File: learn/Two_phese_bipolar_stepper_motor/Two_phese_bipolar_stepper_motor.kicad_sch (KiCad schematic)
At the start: 15 parts

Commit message: 21/02/23 inserito tutti i componenti necessari per il nuovo progetto.
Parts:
- added U?: L297, symbol Driver_Motor:L297
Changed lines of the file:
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@@
     (pin "2")
+  )
+  (symbol (lib_id "Driver_Motor:L297") (at 119.38 99.06 0) (unit 1)
+    (in_bom yes) (on_board yes) (fields_autoplaced)
+    (property "Reference" "U?" (id 0) (at 121.3994 116.84 0)
+      (effects (font (size 1.27 1.27)) (justify left))
+    )
+    (property "Value" "L297" (id 1) (at 121.3994 119.38 0)
+      (effects (font (size 1.27 1.27)) (justify left))
+    )
+    (property "Footprint" "" (id 2) (at 113.03 82.55 0)
+      (effects (font (size 1.27 1.27)) hide)
+    )
+    (property "Datasheet" "www.st.com/resource/en/datasheet/cd00000063.pdf" (id 3) (at 113.03 82.55 0)
+      (effects (font (size 1.27 1.27)) hide)
+    )
+    (pin "11")
+    (pin "12")
+    (pin "13")
+    (pin "14")
+    (pin "15")
+    (pin "16")
+    (pin "17")
+    (pin "18")
+    (pin "19")
+    (pin "20")
+    (pin "1")
+    (pin "10")
+    (pin "2")
+    (pin "3")
+    (pin "4")
+    (pin "5")
+    (pin "6")
+    (pin "7")
+    (pin "8")
+    (pin "9")
   )
   (symbol (lib_id "Device:C") (at 212.09 53.34 0) (unit 1)
@@
       (reference "R?") (unit 1) (value "R") (footprint "")
     )
+    (path "/b420444f-520c-4962-ac46-908b94e46b38"
+      (reference "U?") (unit 1) (value "L297") (footprint "")
+    )
   )

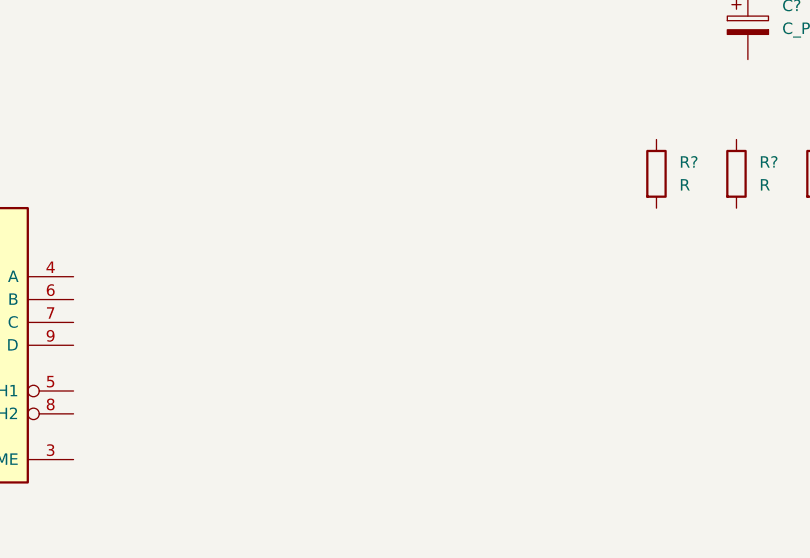
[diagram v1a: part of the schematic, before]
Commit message: 22/02/23 L298N
Ora sono presenti tutti i componenti per creare il progetto.
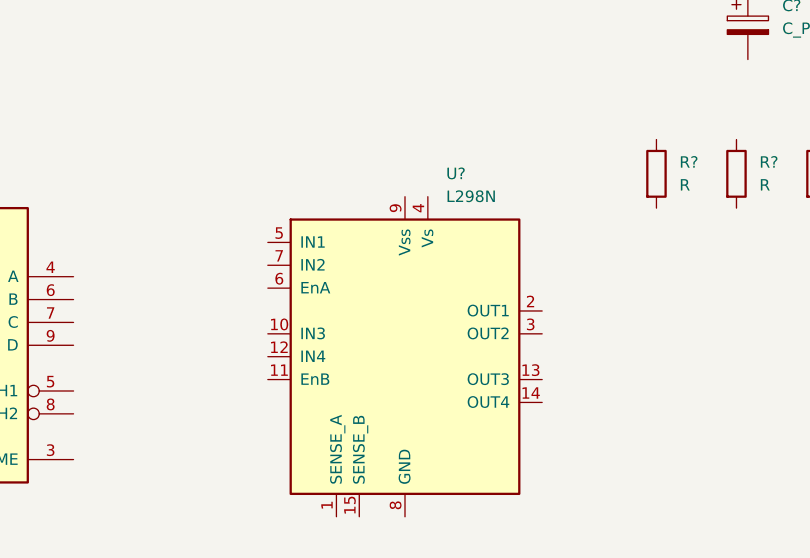
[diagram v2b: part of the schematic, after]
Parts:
- added U?: L298N, Package_TO_SOT_THT:TO-220-15_P2.54x2.54mm_StaggerOdd_Lead4.58mm_Vertical, symbol Driver_Motor:L298N
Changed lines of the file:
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@@
     (pin "2")
+  )
+  (symbol (lib_id "Driver_Motor:L298N") (at 173.99 100.33 0) (unit 1)
+    (in_bom yes) (on_board yes) (fields_autoplaced)
+    (property "Reference" "U?" (id 0) (at 178.5494 80.01 0)
+      (effects (font (size 1.27 1.27)) (justify left))
+    )
+    (property "Value" "L298N" (id 1) (at 178.5494 82.55 0)
+      (effects (font (size 1.27 1.27)) (justify left))
+    )
+    (property "Footprint" "Package_TO_SOT_THT:TO-220-15_P2.54x2.54mm_StaggerOdd_Lead4.58mm_Vertical" (id 2) (at 175.26 116.84 0)
+      (effects (font (size 1.27 1.27)) (justify left) hide)
+    )
+    (property "Datasheet" "http://www.st.com/st-web-ui/static/active/en/resource/technical/document/datasheet/CD00000240.pdf" (id 3) (at 177.8 93.98 0)
+      (effects (font (size 1.27 1.27)) hide)
+    )
+    (pin "1")
+    (pin "10")
+    (pin "11")
+    (pin "12")
+    (pin "13")
+    (pin "14")
+    (pin "15")
+    (pin "2")
+    (pin "3")
+    (pin "4")
+    (pin "5")
+    (pin "6")
+    (pin "7")
+    (pin "8")
+    (pin "9")
   )
   (symbol (lib_id "Device:D_Schottky") (at 137.16 46.99 0) (unit 1)
@@
       (reference "U?") (unit 1) (value "L297") (footprint "")
     )
+    (path "/e37ffe64-a844-4622-840a-a53a0744ab08"
+      (reference "U?") (unit 1) (value "L298N") (footprint "Package_TO_SOT_THT:TO-220-15_P2.54x2.54mm_StaggerOdd_Lead4.58mm_Vertical")
+    )
   )

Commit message: 25/02/23 Inizio collegamento (shc)
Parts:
- C1: renamed from C?; value C -> 3.3nF
- C2, C3: renamed from C?; value C -> 100nF
- C4: renamed from C?; value C_Polarized -> 470uF
- R1: renamed from R?; value R -> 22k
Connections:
- net OSC: now reaches R1.1
- net OSC: now also C1.1
- net VSS: now reaches R1.2
- net VSS: now also C2.1
- net VS: now reaches C4.1
- net VS: now also C3.1
- net GND: now reaches C4.2
- net GND: now also C1.2, C2.2, C3.2
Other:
- moved on the sheet: C1, C2, C3, C4, R1, R?

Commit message: 01/03/23 aggiunto PWR_FLAG
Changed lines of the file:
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@@
   (junction (at 251.46 78.74) (diameter 0) (color 0 0 0 0)
   )
+  (junction (at 214.63 93.98) (diameter 0) (color 0 0 0 0)
+  )
   (junction (at 203.2 81.28) (diameter 0) (color 0 0 0 0)
   )
@@
   (junction (at 218.44 81.28) (diameter 0) (color 0 0 0 0)
   )
+  (junction (at 251.46 76.2) (diameter 0) (color 0 0 0 0)
+  )
+  (junction (at 218.44 80.01) (diameter 0) (color 0 0 0 0)
+  )
   (junction (at 214.63 91.44) (diameter 0) (color 0 0 0 0)
   )
@@
     (stroke (width 0) (type default) (color 0 0 0 0))
   )
+  (wire (pts (xy 245.11 76.2) (xy 251.46 76.2))
+    (stroke (width 0) (type default) (color 0 0 0 0))
+  )
   (wire (pts (xy 242.57 78.74) (xy 251.46 78.74))
     (stroke (width 0) (type default) (color 0 0 0 0))
@@
     (stroke (width 0) (type default) (color 0 0 0 0))
   )
+  (wire (pts (xy 209.55 93.98) (xy 214.63 93.98))
+    (stroke (width 0) (type default) (color 0 0 0 0))
+  )
   (wire (pts (xy 214.63 91.44) (xy 214.63 93.98))
+    (stroke (width 0) (type default) (color 0 0 0 0))
+  )
+  (wire (pts (xy 218.44 80.01) (xy 224.79 80.01))
     (stroke (width 0) (type default) (color 0 0 0 0))
   )
@@
     (pin "2")
   )
+  (symbol (lib_id "power:PWR_FLAG") (at 224.79 80.01 0) (unit 1)
+    (in_bom yes) (on_board yes)
+    (property "Reference" "#FLG?" (id 0) (at 224.79 78.105 0)
+      (effects (font (size 1.27 1.27)) hide)
+    )
+    (property "Value" "PWR_FLAG" (id 1) (at 222.25 76.2 0)
+      (effects (font (size 0.8 0.8)) (justify left))
+    )
+    (property "Footprint" "" (id 2) (at 224.79 80.01 0)
+      (effects (font (size 1.27 1.27)) hide)
+    )
+    (property "Datasheet" "~" (id 3) (at 224.79 80.01 0)
+      (effects (font (size 1.27 1.27)) hide)
+    )
+    (pin "1")
+  )
   (symbol (lib_id "Device:R") (at 209.55 81.28 90) (unit 1)
     (in_bom yes) (on_board yes) (fields_autoplaced)
@@
     (pin "1")
     (pin "2")
+  )
+  (symbol (lib_id "power:PWR_FLAG") (at 245.11 76.2 0) (unit 1)
+    (in_bom yes) (on_board yes) (fields_autoplaced)
+    (property "Reference" "#FLG?" (id 0) (at 245.11 74.295 0)
+      (effects (font (size 1.27 1.27)) hide)
+    )
+    (property "Value" "PWR_FLAG" (id 1) (at 245.11 71.12 0))
+    (property "Footprint" "" (id 2) (at 245.11 76.2 0)
+      (effects (font (size 1.27 1.27)) hide)
+    )
+    (property "Datasheet" "~" (id 3) (at 245.11 76.2 0)
+      (effects (font (size 1.27 1.27)) hide)
+    )
+    (pin "1")
   )
   (symbol (lib_id "power:VSS") (at 218.44 80.01 0) (unit 1)
@@
     (pin "2")
   )
+  (symbol (lib_id "power:PWR_FLAG") (at 209.55 93.98 180) (unit 1)
+    (in_bom yes) (on_board yes)
+    (property "Reference" "#FLG?" (id 0) (at 209.55 95.885 0)
+      (effects (font (size 1.27 1.27)) hide)
+    )
+    (property "Value" "PWR_FLAG" (id 1) (at 212.09 97.79 0)
+      (effects (font (size 0.8 0.8)) (justify left))
+    )
+    (property "Footprint" "" (id 2) (at 209.55 93.98 0)
+      (effects (font (size 1.27 1.27)) hide)
+    )
+    (property "Datasheet" "~" (id 3) (at 209.55 93.98 0)
+      (effects (font (size 1.27 1.27)) hide)
+    )
+    (pin "1")
+  )
   (sheet_instances
     (path "/" (page "1"))
   )
   (symbol_instances
+    (path "/3e6463cb-88fe-4589-b0c8-c0269a2931ca"
+      (reference "#FLG?") (unit 1) (value "PWR_FLAG") (footprint "")
+    )
+    (path "/6791b6c4-8825-4d77-97a1-1f490967f6cd"
+      (reference "#FLG?") (unit 1) (value "PWR_FLAG") (footprint "")
+    )
+    (path "/fbbf62bf-eae9-4a55-9a35-5a034367347f"
+      (reference "#FLG?") (unit 1) (value "PWR_FLAG") (footprint "")
+    )
     (path "/2c34f367-ff20-455d-af43-7cdb3c218d3c"
       (reference "#PWR?") (unit 1) (value "GND") (footprint "")

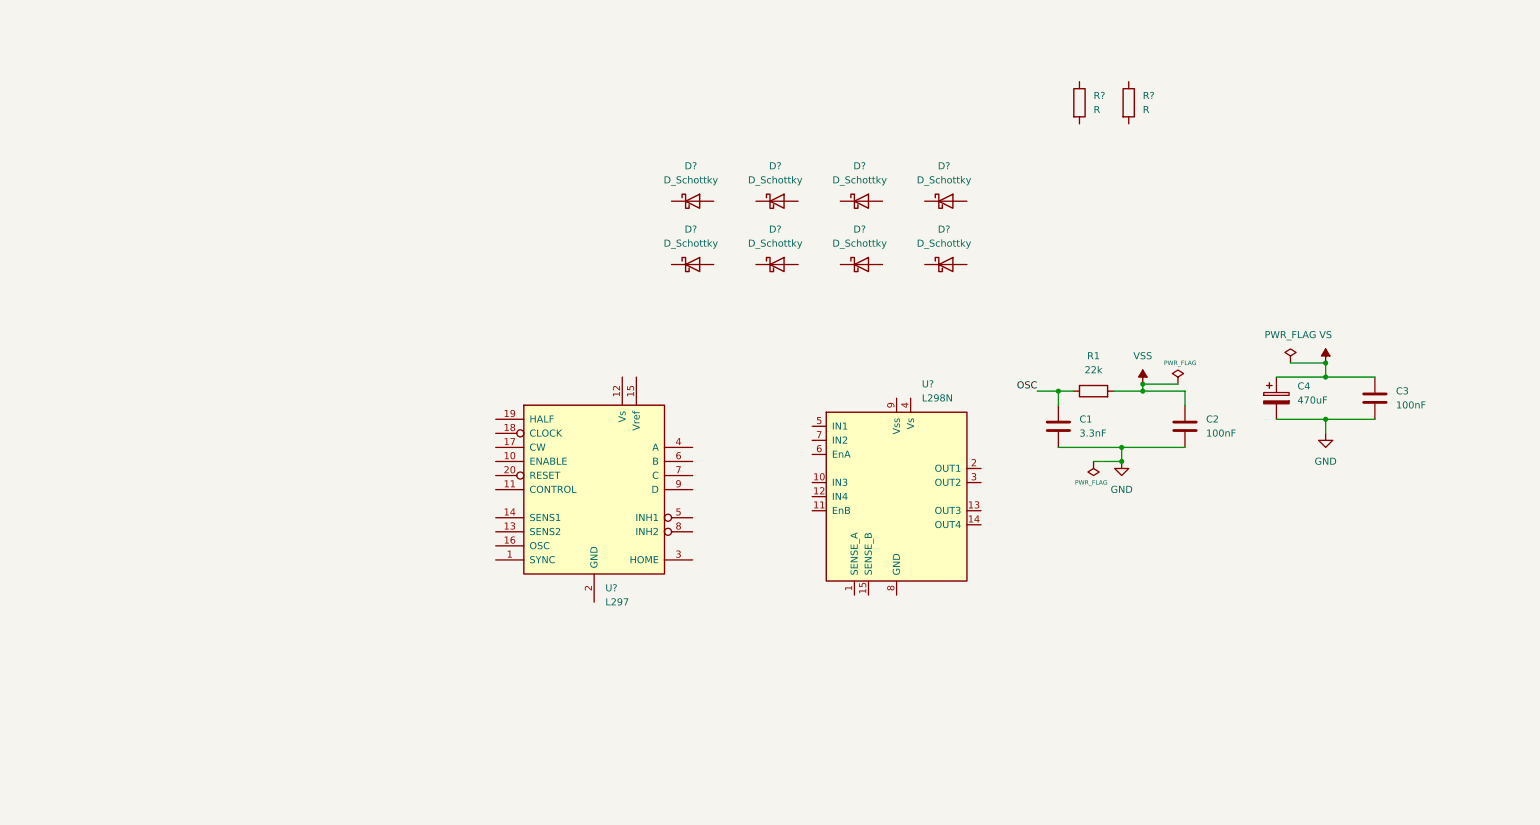
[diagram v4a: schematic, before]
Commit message: 02/03/23 aggiunti diodi Zener
Inizio collegamento del L298N
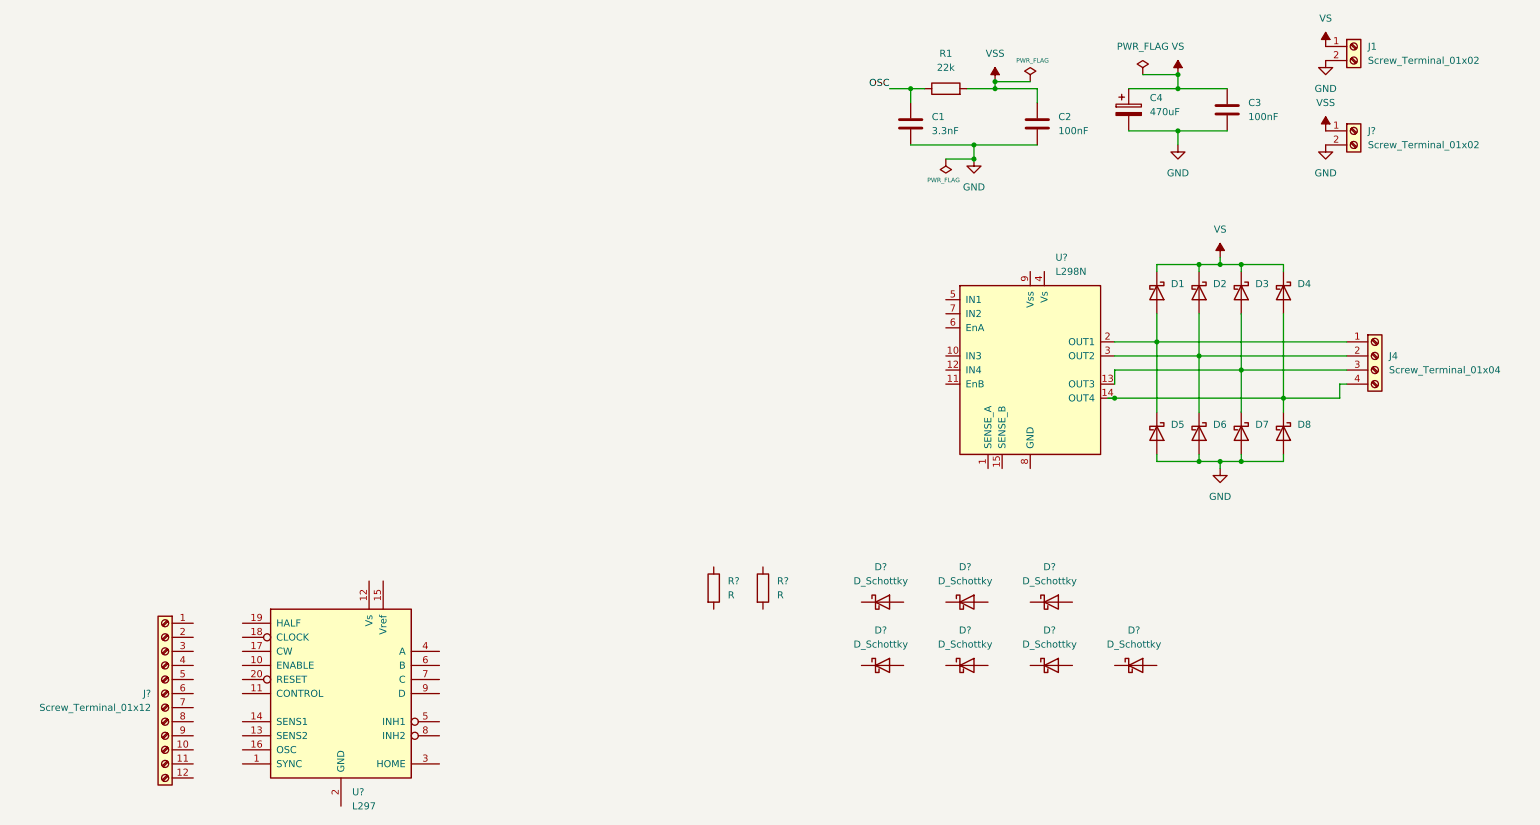
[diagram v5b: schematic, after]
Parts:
- added D2, D3, D4, D5, D6, D7, D8: (no value), symbol Device:D_Schottky
- added J1, J?: Screw_Terminal_01x02, symbol Connector:Screw_Terminal_01x02
- added J4: Screw_Terminal_01x04, symbol Connector:Screw_Terminal_01x04
- added J?: Screw_Terminal_01x12, symbol Connector:Screw_Terminal_01x12
- D1: renamed from D?; value D_Schottky -> (none)
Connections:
- net GND: now also D5.2 (A), D6.2 (A), D7.2 (A), D8.2 (A), J1.2 (Pin_2), J?.2 (Pin_2)
- net VS: now also D1.1 (K), D2.1 (K), D3.1 (K), D4.1 (K), J1.1 (Pin_1)
- net VSS: now also J?.1 (Pin_1)
- net at D1.2 (A): now also U?.2 (OUT1), D5.1 (K), J4.1 (Pin_1)
- net at U?.13 (OUT3): now also D3.2 (A), D7.1 (K), J4.3 (Pin_3)
- net at U?.14 (OUT4): now also D4.2 (A), D8.1 (K), J4.4 (Pin_4)
- net at U?.3 (OUT2): now also D2.2 (A), D6.1 (K), J4.2 (Pin_2)
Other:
- moved on the sheet: C1, C2, C3, C4, D1, D?, R1, R?, U?
